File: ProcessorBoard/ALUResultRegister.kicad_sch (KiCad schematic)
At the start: 2 parts, among them U50 74ABT16374

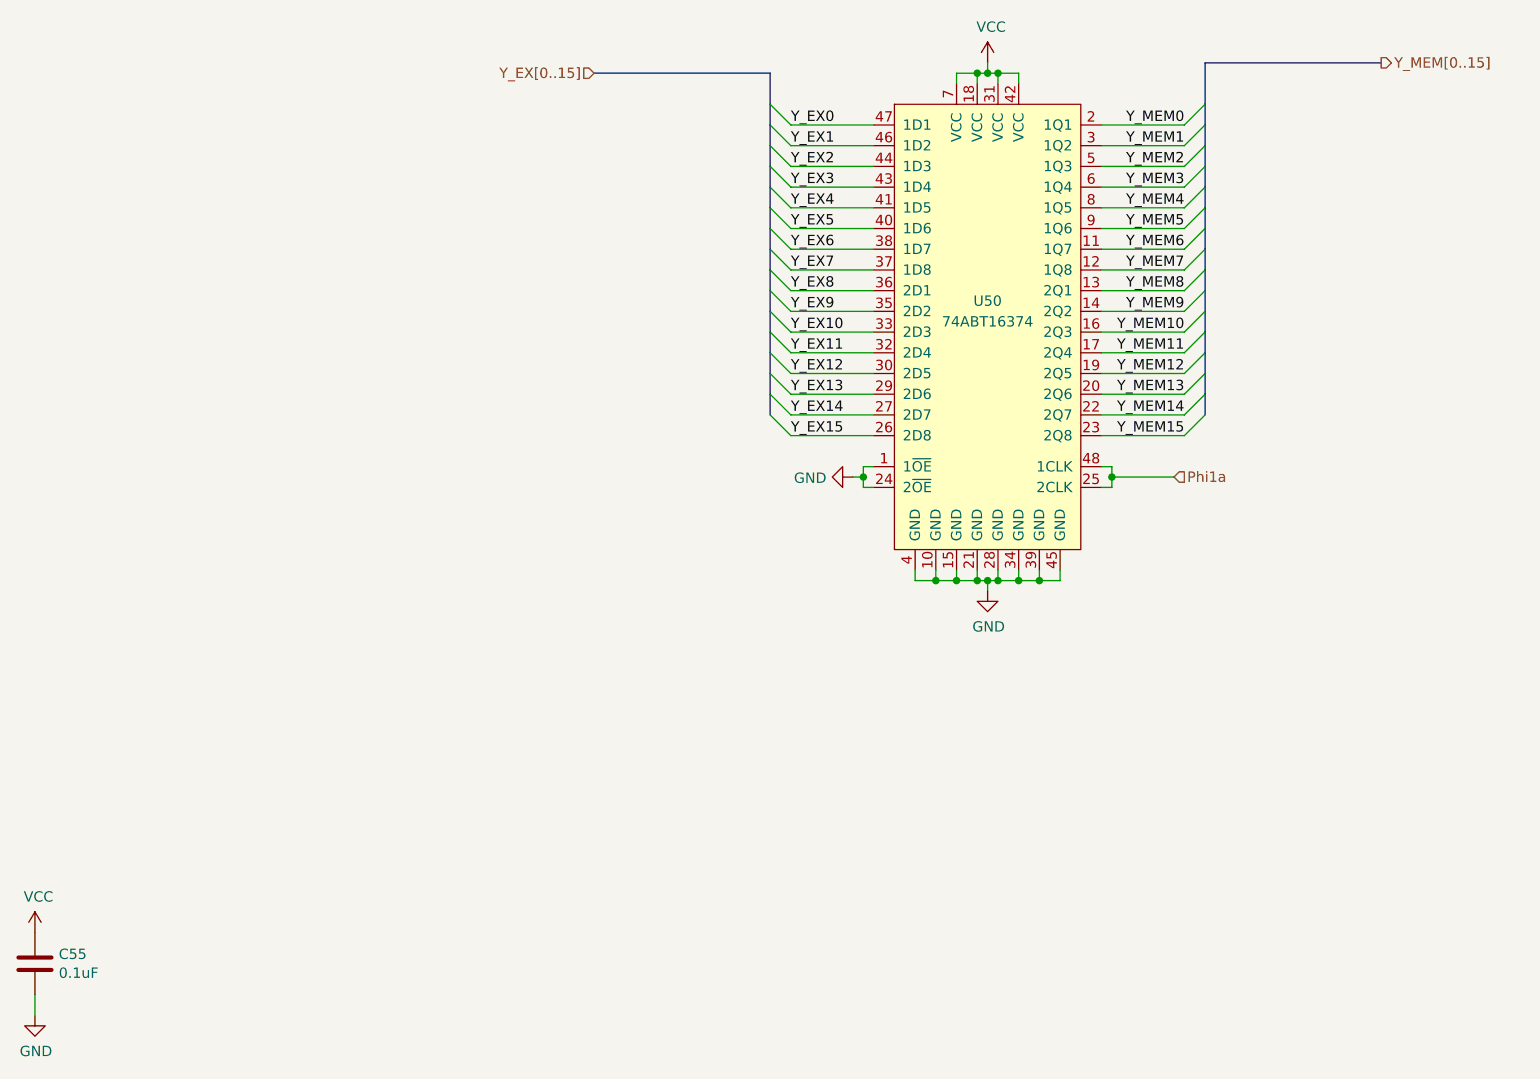
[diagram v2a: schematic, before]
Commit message: ProcessorBoard: update to include M/S bug fix in register file
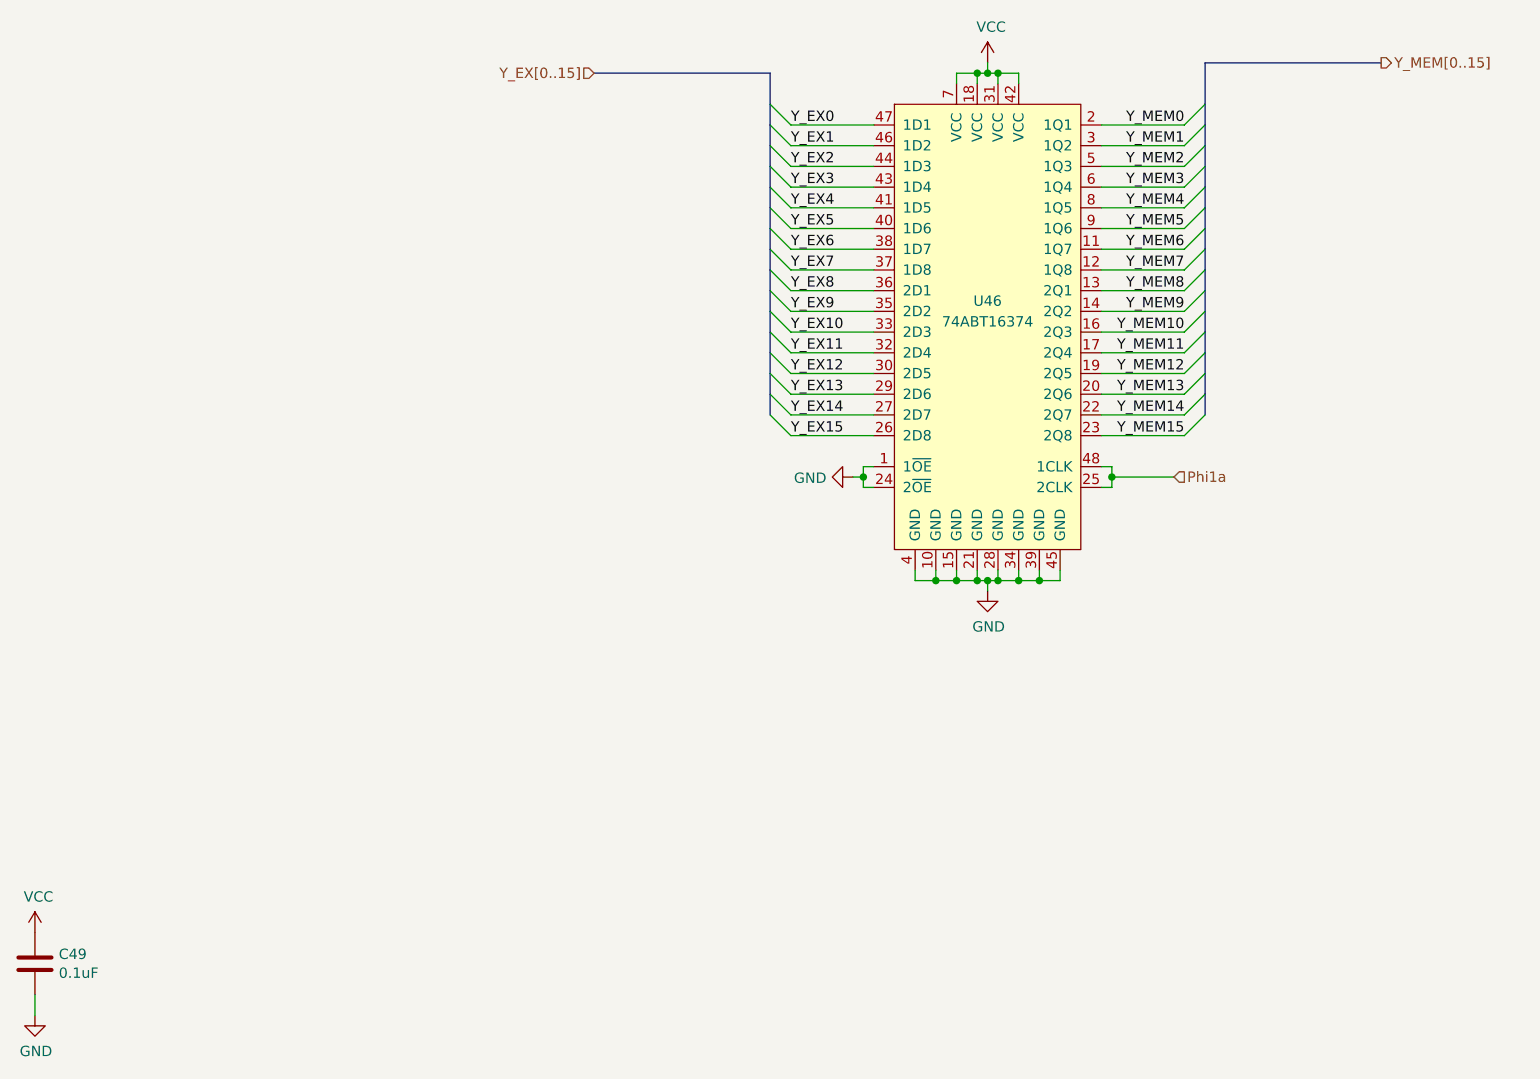
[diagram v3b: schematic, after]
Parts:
- renumbered C55 to C49, U50 to U46
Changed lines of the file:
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@@
   (symbol (lib_id "Device:C") (at 25.4 182.88 0) (unit 1)
     (in_bom yes) (on_board yes) (dnp no)
-    (property "Reference" "C55" (at 28.321 181.7116 0)
+    (property "Reference" "C49" (at 28.321 181.7116 0)
       (effects (font (size 1.27 1.27)) (justify left))
     )
@@
       (project "ProcessorBoard"
         (path "/83c5181e-f5ee-453c-ae5c-d7256ba8837d/00000000-0000-0000-0000-000060a71bbf/00000000-0000-0000-0000-00005fd8d713"
-          (reference "C55") (unit 1)
+          (reference "C49") (unit 1)
         )
       )
@@
   (symbol (lib_id "power:VCC") (at 25.4 179.07 0) (unit 1)
     (in_bom yes) (on_board yes) (dnp no)
-    (property "Reference" "#PWR0334" (at 25.4 182.88 0)
+    (property "Reference" "#PWR0316" (at 25.4 182.88 0)
       (effects (font (size 1.27 1.27)) hide)
     )
@@
       (project "ProcessorBoard"
         (path "/83c5181e-f5ee-453c-ae5c-d7256ba8837d/00000000-0000-0000-0000-000060a71bbf/00000000-0000-0000-0000-00005fd8d713"
-          (reference "#PWR0334") (unit 1)
+          (reference "#PWR0316") (unit 1)
         )
       )
@@
   (symbol (lib_id "power:GND") (at 25.4 189.23 0) (unit 1)
     (in_bom yes) (on_board yes) (dnp no)
-    (property "Reference" "#PWR0335" (at 25.4 195.58 0)
+    (property "Reference" "#PWR0317" (at 25.4 195.58 0)
       (effects (font (size 1.27 1.27)) hide)
     )
@@
       (project "ProcessorBoard"
         (path "/83c5181e-f5ee-453c-ae5c-d7256ba8837d/00000000-0000-0000-0000-000060a71bbf/00000000-0000-0000-0000-00005fd8d713"
-          (reference "#PWR0335") (unit 1)
+          (reference "#PWR0317") (unit 1)
         )
       )
@@
   (symbol (lib_id "power:GND") (at 125.73 123.19 270) (unit 1)
     (in_bom yes) (on_board yes) (dnp no)
-    (property "Reference" "#PWR0336" (at 119.38 123.19 0)
+    (property "Reference" "#PWR0318" (at 119.38 123.19 0)
       (effects (font (size 1.27 1.27)) hide)
     )
@@
       (project "ProcessorBoard"
         (path "/83c5181e-f5ee-453c-ae5c-d7256ba8837d/00000000-0000-0000-0000-000060a71bbf/00000000-0000-0000-0000-00005fd8d713"
-          (reference "#PWR0336") (unit 1)
+          (reference "#PWR0318") (unit 1)
         )
       )
@@
   (symbol (lib_id "power:VCC") (at 142.24 72.39 0) (unit 1)
     (in_bom yes) (on_board yes) (dnp no)
-    (property "Reference" "#PWR0337" (at 142.24 76.2 0)
+    (property "Reference" "#PWR0319" (at 142.24 76.2 0)
       (effects (font (size 1.27 1.27)) hide)
     )
@@
       (project "ProcessorBoard"
         (path "/83c5181e-f5ee-453c-ae5c-d7256ba8837d/00000000-0000-0000-0000-000060a71bbf/00000000-0000-0000-0000-00005fd8d713"
-          (reference "#PWR0337") (unit 1)
+          (reference "#PWR0319") (unit 1)
         )
       )
@@
   (symbol (lib_id "power:GND") (at 142.24 137.16 0) (unit 1)
     (in_bom yes) (on_board yes) (dnp no)
-    (property "Reference" "#PWR0338" (at 142.24 143.51 0)
+    (property "Reference" "#PWR0320" (at 142.24 143.51 0)
       (effects (font (size 1.27 1.27)) hide)
     )
@@
       (project "ProcessorBoard"
         (path "/83c5181e-f5ee-453c-ae5c-d7256ba8837d/00000000-0000-0000-0000-000060a71bbf/00000000-0000-0000-0000-00005fd8d713"
-          (reference "#PWR0338") (unit 1)
+          (reference "#PWR0320") (unit 1)
         )
       )
@@
   (symbol (lib_id "74xx (kicad5):74ABT16374") (at 142.24 101.6 0) (unit 1)
     (in_bom yes) (on_board yes) (dnp no)
-    (property "Reference" "U50" (at 142.24 101.6 0)
+    (property "Reference" "U46" (at 142.24 101.6 0)
       (effects (font (size 1.27 1.27)))
     )
@@
       (project "ProcessorBoard"
         (path "/83c5181e-f5ee-453c-ae5c-d7256ba8837d/00000000-0000-0000-0000-000060a71bbf/00000000-0000-0000-0000-00005fd8d713"
-          (reference "U50") (unit 1)
-        )
-      )
+          (reference "U46") (unit 1)
+        )
+      )

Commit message: ProcessorBoard: Replace Instruction ROM with a header for a daughter board
ROMs will be relocated to a daughter board to allow the memories and their
sockets to be swapped easily.
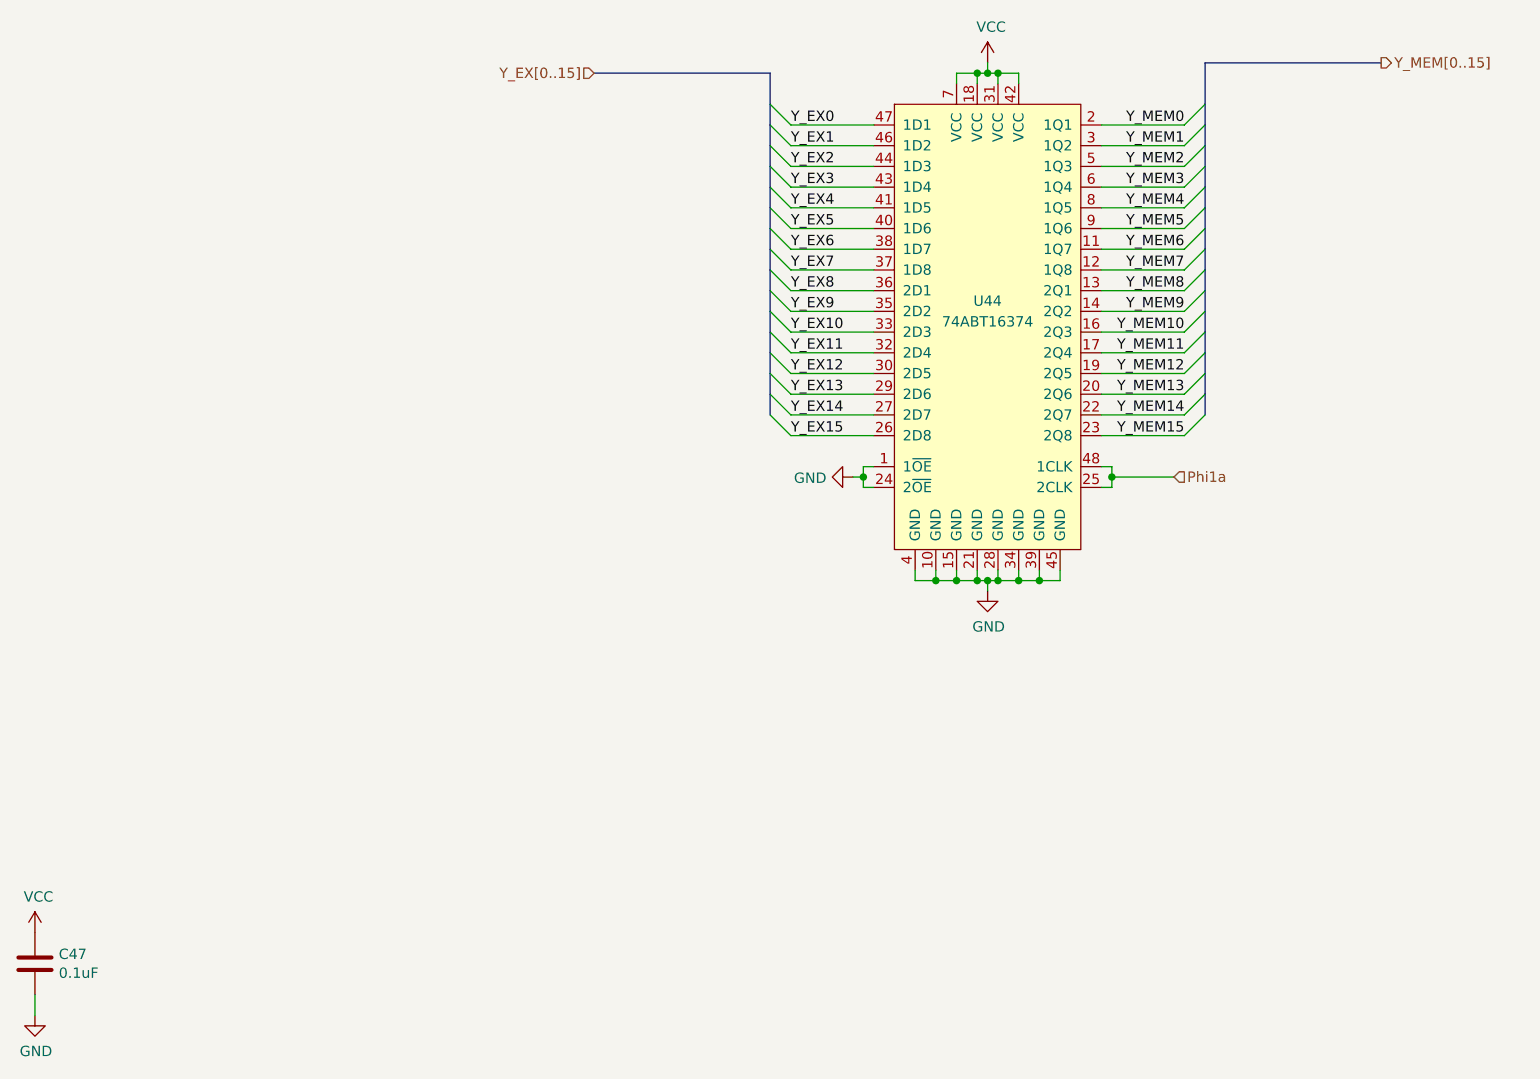
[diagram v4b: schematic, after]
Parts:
- renumbered C49 to C47, U46 to U44
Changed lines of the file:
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@@
   (symbol (lib_id "Device:C") (at 25.4 182.88 0) (unit 1)
     (in_bom yes) (on_board yes) (dnp no)
-    (property "Reference" "C49" (at 28.321 181.7116 0)
+    (property "Reference" "C47" (at 28.321 181.7116 0)
       (effects (font (size 1.27 1.27)) (justify left))
     )
@@
       (project "ProcessorBoard"
         (path "/83c5181e-f5ee-453c-ae5c-d7256ba8837d/00000000-0000-0000-0000-000060a71bbf/00000000-0000-0000-0000-00005fd8d713"
-          (reference "C49") (unit 1)
+          (reference "C47") (unit 1)
         )
       )
@@
   (symbol (lib_id "power:VCC") (at 25.4 179.07 0) (unit 1)
     (in_bom yes) (on_board yes) (dnp no)
-    (property "Reference" "#PWR0316" (at 25.4 182.88 0)
+    (property "Reference" "#PWR0308" (at 25.4 182.88 0)
       (effects (font (size 1.27 1.27)) hide)
     )
@@
       (project "ProcessorBoard"
         (path "/83c5181e-f5ee-453c-ae5c-d7256ba8837d/00000000-0000-0000-0000-000060a71bbf/00000000-0000-0000-0000-00005fd8d713"
-          (reference "#PWR0316") (unit 1)
+          (reference "#PWR0308") (unit 1)
         )
       )
@@
   (symbol (lib_id "power:GND") (at 25.4 189.23 0) (unit 1)
     (in_bom yes) (on_board yes) (dnp no)
-    (property "Reference" "#PWR0317" (at 25.4 195.58 0)
+    (property "Reference" "#PWR0309" (at 25.4 195.58 0)
       (effects (font (size 1.27 1.27)) hide)
     )
@@
       (project "ProcessorBoard"
         (path "/83c5181e-f5ee-453c-ae5c-d7256ba8837d/00000000-0000-0000-0000-000060a71bbf/00000000-0000-0000-0000-00005fd8d713"
-          (reference "#PWR0317") (unit 1)
+          (reference "#PWR0309") (unit 1)
         )
       )
@@
   (symbol (lib_id "power:GND") (at 125.73 123.19 270) (unit 1)
     (in_bom yes) (on_board yes) (dnp no)
-    (property "Reference" "#PWR0318" (at 119.38 123.19 0)
+    (property "Reference" "#PWR0310" (at 119.38 123.19 0)
       (effects (font (size 1.27 1.27)) hide)
     )
@@
       (project "ProcessorBoard"
         (path "/83c5181e-f5ee-453c-ae5c-d7256ba8837d/00000000-0000-0000-0000-000060a71bbf/00000000-0000-0000-0000-00005fd8d713"
-          (reference "#PWR0318") (unit 1)
+          (reference "#PWR0310") (unit 1)
         )
       )
@@
   (symbol (lib_id "power:VCC") (at 142.24 72.39 0) (unit 1)
     (in_bom yes) (on_board yes) (dnp no)
-    (property "Reference" "#PWR0319" (at 142.24 76.2 0)
+    (property "Reference" "#PWR0311" (at 142.24 76.2 0)
       (effects (font (size 1.27 1.27)) hide)
     )
@@
       (project "ProcessorBoard"
         (path "/83c5181e-f5ee-453c-ae5c-d7256ba8837d/00000000-0000-0000-0000-000060a71bbf/00000000-0000-0000-0000-00005fd8d713"
-          (reference "#PWR0319") (unit 1)
+          (reference "#PWR0311") (unit 1)
         )
       )
@@
   (symbol (lib_id "power:GND") (at 142.24 137.16 0) (unit 1)
     (in_bom yes) (on_board yes) (dnp no)
-    (property "Reference" "#PWR0320" (at 142.24 143.51 0)
+    (property "Reference" "#PWR0312" (at 142.24 143.51 0)
       (effects (font (size 1.27 1.27)) hide)
     )
@@
       (project "ProcessorBoard"
         (path "/83c5181e-f5ee-453c-ae5c-d7256ba8837d/00000000-0000-0000-0000-000060a71bbf/00000000-0000-0000-0000-00005fd8d713"
-          (reference "#PWR0320") (unit 1)
+          (reference "#PWR0312") (unit 1)
         )
       )
@@
   (symbol (lib_id "74xx (kicad5):74ABT16374") (at 142.24 101.6 0) (unit 1)
     (in_bom yes) (on_board yes) (dnp no)
-    (property "Reference" "U46" (at 142.24 101.6 0)
+    (property "Reference" "U44" (at 142.24 101.6 0)
       (effects (font (size 1.27 1.27)))
     )
@@
       (project "ProcessorBoard"
         (path "/83c5181e-f5ee-453c-ae5c-d7256ba8837d/00000000-0000-0000-0000-000060a71bbf/00000000-0000-0000-0000-00005fd8d713"
-          (reference "U46") (unit 1)
-        )
-      )
+          (reference "U44") (unit 1)
+        )
+      )

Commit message: ProcessorBoard: Copy symbols into project symbol library, make consistent
Symbols created for Turtle16 have been copied into a project-specific
symbol library. The symbols have all been updated with manufacturer,
manufacturer part number, mouser part number, and digikey part number.

Test points and mounting holes have been marked to be excluded from BOM.
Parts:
- C47: footprint Capacitor_SMD:C_0603_1608Metric_Pad1.08x0.95mm_HandSolder -> Capacitor_SMD:C_0603_1608Metric; Digikey# (none) -> 587-6004-1-ND; Manufacturer (none) -> Taiyo Yuden; Manufacturer# (none) -> EMK107B7104KAHT; Mouser https://www.mouser.com/ProductDetail/963-EMK107B7104KAHT -> (none)
- U44: symbol 74xx (kicad5):74ABT16374 -> Turtle16:74ABT16374; Digikey# (none) -> 296-3900-1-ND; Manufacturer (none) -> Texas Instruments; Manufacturer# (none) -> SN74ABT16374ADGGR; Mouser https://www.mouser.com/ProductDetail/Texas-Instruments/SN74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 -> (none); Mouser# (none) -> 595-SNABT16374ADGGR
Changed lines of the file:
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@@
   (title_block
     (title "EX/MEM: ALUResult Register")
-    (date "2023-11-20")
+    (date "2023-11-25")
     (rev "A")
   )
@@
       (effects (font (size 1.27 1.27)) (justify left))
     )
-    (property "Footprint" "Capacitor_SMD:C_0603_1608Metric_Pad1.08x0.95mm_HandSolder" (at 26.3652 186.69 0)
-      (effects (font (size 1.27 1.27)) hide)
-    )
-    (property "Datasheet" "~" (at 25.4 182.88 0)
-      (effects (font (size 1.27 1.27)) hide)
-    )
-    (property "Mouser" "https://www.mouser.com/ProductDetail/963-EMK107B7104KAHT" (at 25.4 182.88 0)
+    (property "Footprint" "Capacitor_SMD:C_0603_1608Metric" (at 128.5748 82.55 0)
+      (effects (font (size 1.27 1.27)) hide)
+    )
+    (property "Datasheet" "https://www.mouser.com/datasheet/2/396/taiyo_yuden_12132018_mlcc11_hq_e-1510082.pdf" (at 129.54 78.74 0)
+      (effects (font (size 1.27 1.27)) hide)
+    )
+    (property "Manufacturer" "Taiyo Yuden" (at 129.54 78.74 0)
+      (effects (font (size 1.27 1.27)) hide)
+    )
+    (property "Manufacturer#" "EMK107B7104KAHT" (at 129.54 78.74 0)
+      (effects (font (size 1.27 1.27)) hide)
+    )
+    (property "Digikey#" "587-6004-1-ND" (at 129.54 78.74 0)
       (effects (font (size 1.27 1.27)) hide)
     )
@@
     )
   )
-  (symbol (lib_id "74xx (kicad5):74ABT16374") (at 142.24 101.6 0) (unit 1)
+  (symbol (lib_id "Turtle16:74ABT16374") (at 142.24 101.6 0) (unit 1)
     (in_bom yes) (on_board yes) (dnp no)
     (property "Reference" "U44" (at 142.24 101.6 0)
@@
       (effects (font (size 1.27 1.27)) hide)
     )
-    (property "Datasheet" "https://www.ti.com/lit/ds/symlink/sn74abt16374a.pdf?HQS=dis-mous-null-mousermode-dsf-pf-null-wwe&ts=1617318801237" (at 153.67 118.11 0)
-      (effects (font (size 1.27 1.27)) hide)
-    )
-    (property "Mouser" "https://www.mouser.com/ProductDetail/Texas-Instruments/SN74ABT16374ADGGR?qs=%2Fha2pyFadui8Wf%2F61v2joCyY9bOa3peBR5btn0VUHs8%3D" (at 142.24 109.22 0)
-      (effects (font (size 1.27 1.27)) hide)
-    )
+    (property "Datasheet" "https://www.ti.com/general/docs/suppproductinfo.tsp?distId=26&gotoUrl=https://www.ti.com/lit/gpn/sn74abt16374a" (at 153.67 118.11 0)
+      (effects (font (size 1.27 1.27)) hide)
+    )
+    (property "Manufacturer" "Texas Instruments" (at 142.24 101.6 0)
+      (effects (font (size 1.27 1.27)) hide)
+    )
+    (property "Manufacturer#" "SN74ABT16374ADGGR" (at 142.24 101.6 0)
+      (effects (font (size 1.27 1.27)) hide)
+    )
+    (property "Mouser#" "595-SNABT16374ADGGR" (at 142.24 101.6 0)
+      (effects (font (size 1.27 1.27)) hide)
+    )
+    (property "Digikey#" "296-3900-1-ND" (at 142.24 101.6 0)
+      (effects (font (size 1.27 1.27)) hide)
+    )
